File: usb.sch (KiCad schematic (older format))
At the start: 15 parts, among them J2 USB_OTG, Q1 BC817, U1 STMPS2151STR

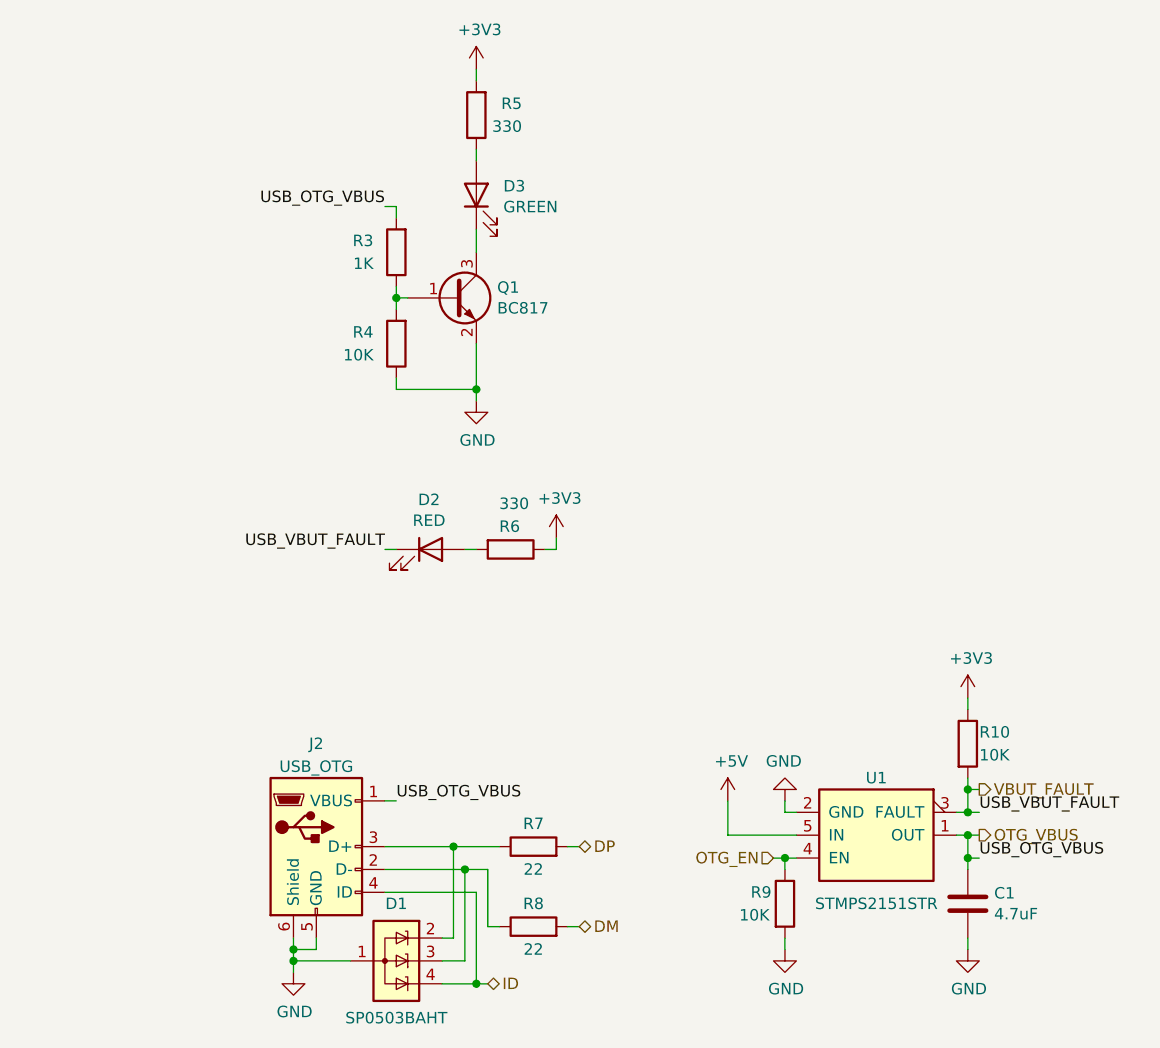
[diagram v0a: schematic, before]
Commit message: Запитал МК, добавил цепи питания, тактирования, модуль клавиатуры.
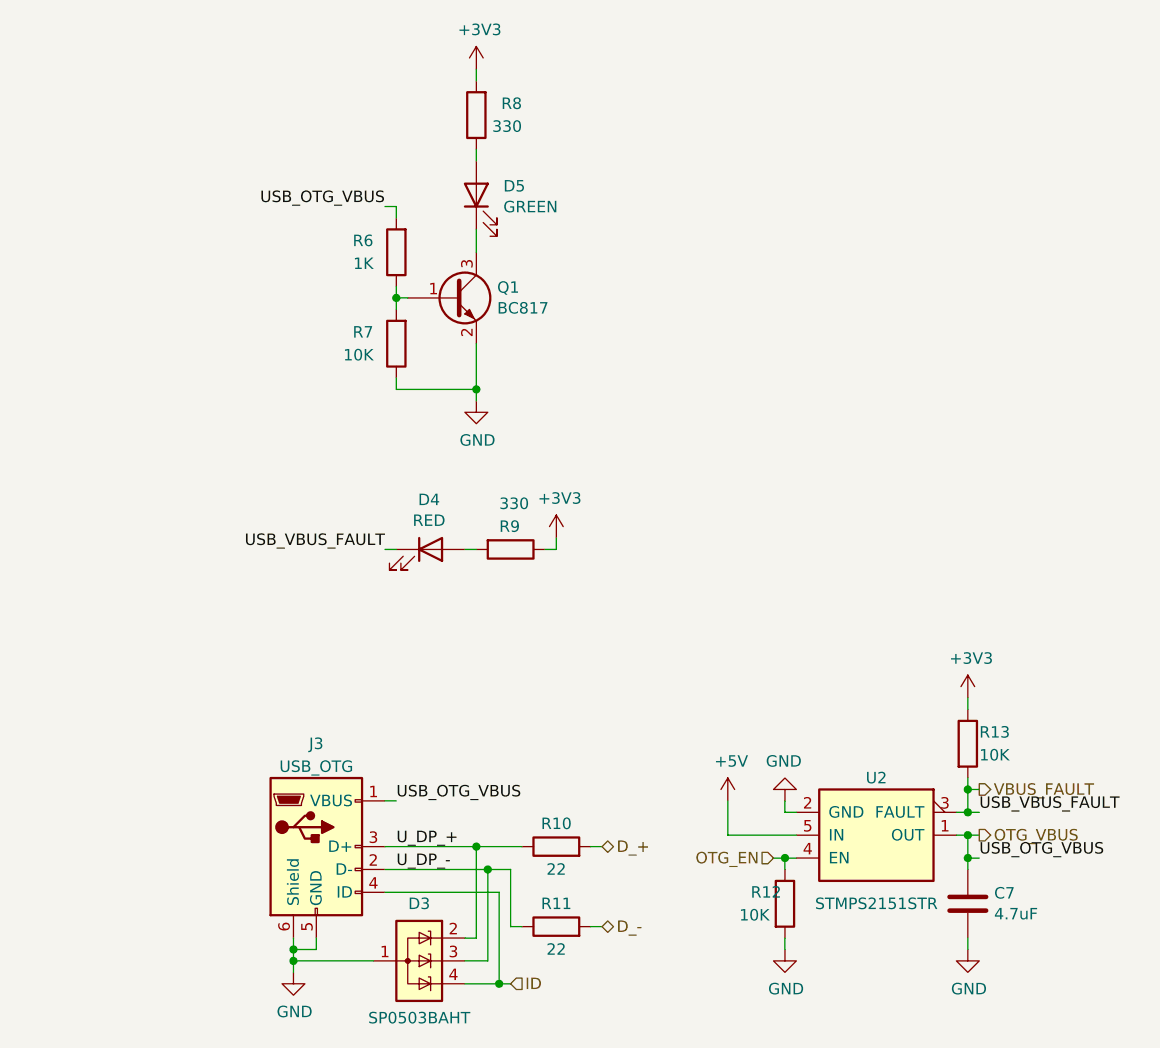
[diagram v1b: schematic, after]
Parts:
- renumbered C1 to C7, D1 to D3, D2 to D4, D3 to D5, J2 to J3, R7 to R10, R8 to R11, R9 to R12, R10 to R13, R3 to R6, R4 to R7, R5 to R8, R6 to R9, U1 to U2
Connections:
- net U_DP_-: now reaches D3.3 (K), J3.2 (D-), R11.1
- net U_DP_+: now reaches D3.2 (K), J3.3 (D+), R10.1
- net DM renamed D_-
- net DP renamed D_+
- net VBUT_FAULT renamed VBUS_FAULT
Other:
- moved on the sheet: D3, R10, R11
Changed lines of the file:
@@
 $Descr A4 11693 8268
 encoding utf-8
-Sheet 5 5
+Sheet 9 9
 Title ""
 Date ""
@@
 $EndDescr
 $Comp
-L interface_usb:STMPS2151STR U1
+L interface_usb:STMPS2151STR U2
 U 1 1 5EBF34AD
 P 6900 4550
-F 0 "U1" H 7150 4600 50  0000 C CNN
+F 0 "U2" H 7150 4600 50  0000 C CNN
 F 1 "STMPS2151STR" H 7150 4050 50  0000 C CNN
 F 2 "Package_TO_SOT_SMD:SOT-23-5_HandSoldering" H 6950 4600 50  0001 C CNN
@@
 $EndComp
 $Comp
-L power:GND #PWR014
+L power:GND #PWR017
 U 1 1 5EBF34B3
 P 6750 4600
-F 0 "#PWR014" H 6750 4350 50  0001 C CNN
+F 0 "#PWR017" H 6750 4350 50  0001 C CNN
 F 1 "GND" H 6755 4427 50  0000 C CNN
 F 2 "" H 6750 4600 50  0001 C CNN
@@
 	6750 4650 6750 4600
 $Comp
-L power:+5V #PWR013
+L power:+5V #PWR016
 U 1 1 5EBF34BB
 P 6500 4600
-F 0 "#PWR013" H 6500 4450 50  0001 C CNN
+F 0 "#PWR016" H 6500 4450 50  0001 C CNN
 F 1 "+5V" H 6515 4773 50  0000 C CNN
 F 2 "" H 6500 4600 50  0001 C CNN
@@
 	7500 4750 7550 4750
 $Comp
-L Device:R R9
+L Device:R R12
 U 1 1 5EBF34C5
 P 6750 5050
-F 0 "R9" H 6600 5100 50  0000 L CNN
+F 0 "R12" H 6600 5100 50  0000 L CNN
 F 1 "10K" H 6550 5000 50  0000 L CNN
 F 2 "Resistor_SMD:R_0603_1608Metric_Pad1.05x0.95mm_HandSolder" V 6680 5050 50  0001 C CNN
@@
 	6750 4850 6750 4900
 $Comp
-L power:GND #PWR015
+L power:GND #PWR018
 U 1 1 5EBF34CD
 P 6750 5250
-F 0 "#PWR015" H 6750 5000 50  0001 C CNN
+F 0 "#PWR018" H 6750 5000 50  0001 C CNN
 F 1 "GND" H 6755 5077 50  0000 C CNN
 F 2 "" H 6750 5250 50  0001 C CNN
@@
 Connection ~ 6750 4850
 $Comp
-L Device:C C1
+L Device:C C7
 U 1 1 5EBF34D7
 P 7550 5050
-F 0 "C1" H 7665 5096 50  0000 L CNN
+F 0 "C7" H 7665 5096 50  0000 L CNN
 F 1 "4.7uF" H 7665 5005 50  0000 L CNN
 F 2 "Capacitor_SMD:C_0603_1608Metric_Pad1.05x0.95mm_HandSolder" H 7588 4900 50  0001 C CNN
@@
 Connection ~ 7550 4750
 $Comp
-L power:GND #PWR017
+L power:GND #PWR020
 U 1 1 5EBF34E0
 P 7550 5250
-F 0 "#PWR017" H 7550 5000 50  0001 C CNN
+F 0 "#PWR020" H 7550 5000 50  0001 C CNN
 F 1 "GND" H 7555 5077 50  0000 C CNN
 F 2 "" H 7550 5250 50  0001 C CNN
@@
 	7500 4650 7550 4650
 $Comp
-L power:+3V3 #PWR016
+L power:+3V3 #PWR019
 U 1 1 5EBF34E9
 P 7550 4150
-F 0 "#PWR016" H 7550 4000 50  0001 C CNN
+F 0 "#PWR019" H 7550 4000 50  0001 C CNN
 F 1 "+3V3" H 7565 4323 50  0000 C CNN
 F 2 "" H 7550 4150 50  0001 C CNN
@@
 	7550 4150 7550 4200
 $Comp
-L Device:LED D2
+L Device:LED D4
 U 1 1 5EBF34F9
 P 5200 3500
-F 0 "D2" H 5193 3717 50  0000 C CNN
+F 0 "D4" H 5193 3717 50  0000 C CNN
 F 1 "RED" H 5193 3626 50  0000 C CNN
 F 2 "LED_SMD:LED_0603_1608Metric_Pad1.05x0.95mm_HandSolder" H 5200 3500 50  0001 C CNN
@@
 $EndComp
 $Comp
-L Device:R R6
+L Device:R R9
 U 1 1 5EBF34FF
 P 5550 3500
-F 0 "R6" V 5450 3450 50  0000 L CNN
+F 0 "R9" V 5450 3450 50  0000 L CNN
 F 1 "330" V 5350 3450 50  0000 L CNN
 F 2 "Resistor_SMD:R_0603_1608Metric_Pad1.05x0.95mm_HandSolder" V 5480 3500 50  0001 C CNN
@@
 $EndComp
 $Comp
-L power:+3V3 #PWR012
+L power:+3V3 #PWR015
 U 1 1 5EBF3506
 P 5750 3450
-F 0 "#PWR012" H 5750 3300 50  0001 C CNN
+F 0 "#PWR015" H 5750 3300 50  0001 C CNN
 F 1 "+3V3" H 5765 3623 50  0000 C CNN
 F 2 "" H 5750 3450 50  0001 C CNN
@@
 	5750 3500 5750 3450
 $Comp
-L Device:R R3
+L Device:R R6
 U 1 1 5EBF3510
 P 5050 2200
-F 0 "R3" H 5150 2150 50  0000 L CNN
+F 0 "R6" H 5150 2150 50  0000 L CNN
 F 1 "1K" H 5150 2250 50  0000 L CNN
 F 2 "Resistor_SMD:R_0603_1608Metric_Pad1.05x0.95mm_HandSolder" V 4980 2200 50  0001 C CNN
@@
 $EndComp
 $Comp
-L Device:R R4
+L Device:R R7
 U 1 1 5EBF3516
 P 5050 2600
-F 0 "R4" H 5150 2550 50  0000 L CNN
+F 0 "R7" H 5150 2550 50  0000 L CNN
 F 1 "10K" H 5150 2650 50  0000 L CNN
 F 2 "Resistor_SMD:R_0603_1608Metric_Pad1.05x0.95mm_HandSolder" V 4980 2600 50  0001 C CNN
@@
 $EndComp
 $Comp
-L Device:R R5
+L Device:R R8
 U 1 1 5EBF351C
 P 5400 1600
-F 0 "R5" H 5200 1550 50  0000 L CNN
+F 0 "R8" H 5200 1550 50  0000 L CNN
 F 1 "330" H 5200 1650 50  0000 L CNN
 F 2 "Resistor_SMD:R_0603_1608Metric_Pad1.05x0.95mm_HandSolder" V 5330 1600 50  0001 C CNN
@@
 Connection ~ 5050 2400
 $Comp
-L power:+3V3 #PWR010
+L power:+3V3 #PWR013
 U 1 1 5EBF352C
 P 5400 1400
-F 0 "#PWR010" H 5400 1250 50  0001 C CNN
+F 0 "#PWR013" H 5400 1250 50  0001 C CNN
 F 1 "+3V3" H 5415 1573 50  0000 C CNN
 F 2 "" H 5400 1400 50  0001 C CNN
@@
 	5400 1400 5400 1450
 $Comp
-L Device:LED D3
+L Device:LED D5
 U 1 1 5EBF3533
 P 5400 1950
-F 0 "D3" V 5439 1832 50  0000 R CNN
+F 0 "D5" V 5439 1832 50  0000 R CNN
 F 1 "GREEN" V 5348 1832 50  0000 R CNN
 F 2 "LED_SMD:LED_0603_1608Metric_Pad1.05x0.95mm_HandSolder" H 5400 1950 50  0001 C CNN
@@
 	5400 2100 5400 2200
 $Comp
-L power:GND #PWR011
+L power:GND #PWR014
 U 1 1 5EBF3541
 P 5400 2850
-F 0 "#PWR011" H 5400 2600 50  0001 C CNN
+F 0 "#PWR014" H 5400 2600 50  0001 C CNN
 F 1 "GND" H 5405 2677 50  0000 C CNN
 F 2 "" H 5400 2850 50  0001 C CNN
@@
 	5050 2000 5050 2050
 $Comp
-L Connector:USB_OTG J2
+L Connector:USB_OTG J3
 U 1 1 5EBF354C
 P 4700 4800
-F 0 "J2" H 4700 5250 50  0000 C CNN
+F 0 "J3" H 4700 5250 50  0000 C CNN
 F 1 "USB_OTG" H 4700 5150 50  0000 C CNN
 F 2 "Connector_USB:USB_Mini-B_Wuerth_65100516121_Horizontal" H 4850 4750 50  0001 C CNN
@@
 $EndComp
 Wire Wire Line
-	5000 4800 5300 4800
-Wire Wire Line
-	5300 5200 5300 4800
-Connection ~ 5300 4800
-Wire Wire Line
-	5300 4800 5500 4800
+	5000 4800 5400 4800
+Wire Wire Line
+	5400 5200 5400 4800
+Connection ~ 5400 4800
+Wire Wire Line
+	5400 4800 5600 4800
 Connection ~ 4600 5300
 Wire Wire Line
 	4600 5350 4600 5300
 Wire Wire Line
-	4600 5300 4850 5300
-Wire Wire Line
-	5350 4900 5450 4900
-Connection ~ 5350 4900
-Wire Wire Line
-	5350 5300 5350 4900
-Wire Wire Line
-	5250 5300 5350 5300
-Wire Wire Line
-	5250 5200 5300 5200
-Connection ~ 5400 5400
-Wire Wire Line
-	5250 5400 5400 5400
-Wire Wire Line
-	5000 5000 5400 5000
-Wire Wire Line
-	5400 5400 5450 5400
-Wire Wire Line
-	5400 5000 5400 5400
-Wire Wire Line
-	5800 5150 5850 5150
-Wire Wire Line
-	5800 4800 5850 4800
-Wire Wire Line
-	5450 5150 5500 5150
-Wire Wire Line
-	5450 4900 5450 5150
-Wire Wire Line
-	5000 4900 5350 4900
-$Comp
-L Device:R R7
+	4600 5300 4950 5300
+Wire Wire Line
+	5450 4900 5550 4900
+Connection ~ 5450 4900
+Wire Wire Line
+	5450 5300 5450 4900
+Connection ~ 5500 5400
+Wire Wire Line
+	5350 5400 5500 5400
+Wire Wire Line
+	5000 5000 5500 5000
+Wire Wire Line
+	5500 5400 5550 5400
+Wire Wire Line
+	5500 5000 5500 5400
+Wire Wire Line
+	5900 5150 5950 5150
+Wire Wire Line
+	5900 4800 5950 4800
+Wire Wire Line
+	5550 5150 5600 5150
+Wire Wire Line
+	5550 4900 5550 5150
+Wire Wire Line
+	5000 4900 5450 4900
+$Comp
+L Device:R R10
 U 1 1 5EBF356B
-P 5650 4800
-F 0 "R7" V 5750 4800 50  0000 C CNN
-F 1 "22" V 5550 4800 50  0000 C CNN
-F 2 "Resistor_SMD:R_0603_1608Metric_Pad1.05x0.95mm_HandSolder" V 5580 4800 50  0001 C CNN
-F 3 "~" H 5650 4800 50  0001 C CNN
-	1    5650 4800
+P 5750 4800
+F 0 "R10" V 5850 4800 50  0000 C CNN
+F 1 "22" V 5650 4800 50  0000 C CNN
+F 2 "Resistor_SMD:R_0603_1608Metric_Pad1.05x0.95mm_HandSolder" V 5680 4800 50  0001 C CNN
+F 3 "~" H 5750 4800 50  0001 C CNN
+	1    5750 4800
 	0    -1   -1   0
 $EndComp
@@
 	4600 5300 4600 5250
 $Comp
-L power:GND #PWR08
+L power:GND #PWR012
 U 1 1 5EBF3573
 P 4600 5350
-F 0 "#PWR08" H 4600 5100 50  0001 C CNN
+F 0 "#PWR012" H 4600 5100 50  0001 C CNN
 F 1 "GND" H 4605 5177 50  0000 C CNN
 F 2 "" H 4600 5350 50  0001 C CNN
@@
 	4600 5200 4600 5250
 $Comp
-L Power_Protection:SP0503BAHT D1
+L Power_Protection:SP0503BAHT D3
 U 1 1 5EBF357C
-P 5050 5300
-F 0 "D1" V 4800 5300 50  0000 C CNN
-F 1 "SP0503BAHT" V 5300 5300 50  0000 C CNN
-F 2 "Package_TO_SOT_SMD:SOT-143_Handsoldering" H 5275 5250 50  0001 L CNN
-F 3 "http://www.littelfuse.com/~/media/files/littelfuse/technical%20resources/documents/data%20sheets/sp05xxba.pdf" H 5175 5425 50  0001 C CNN
-	1    5050 5300
+P 5150 5300
+F 0 "D3" V 4900 5300 50  0000 C CNN
+F 1 "SP0503BAHT" V 5400 5300 50  0000 C CNN
+F 2 "Package_TO_SOT_SMD:SOT-143_Handsoldering" H 5375 5250 50  0001 L CNN
+F 3 "http://www.littelfuse.com/~/media/files/littelfuse/technical%20resources/documents/data%20sheets/sp05xxba.pdf" H 5275 5425 50  0001 C CNN
+	1    5150 5300
 	0    1    1    0
 $EndComp
 $Comp
-L Device:R R8
+L Device:R R11
 U 1 1 5EBF3583
-P 5650 5150
-F 0 "R8" V 5750 5150 50  0000 C CNN
-F 1 "22" V 5550 5150 50  0000 C CNN
-F 2 "Resistor_SMD:R_0603_1608Metric_Pad1.05x0.95mm_HandSolder" V 5580 5150 50  0001 C CNN
-F 3 "~" H 5650 5150 50  0001 C CNN
-	1    5650 5150
+P 5750 5150
+F 0 "R11" V 5850 5150 50  0000 C CNN
+F 1 "22" V 5650 5150 50  0000 C CNN
+F 2 "Resistor_SMD:R_0603_1608Metric_Pad1.05x0.95mm_HandSolder" V 5680 5150 50  0001 C CNN
+F 3 "~" H 5750 5150 50  0001 C CNN
+	1    5750 5150
 	0    -1   -1   0
 $EndComp
@@
 	5000 4600 5050 4600
 Text HLabel 7600 4550 2    50   Output ~ 0
-VBUT_FAULT
+VBUS_FAULT
 Text HLabel 7600 4750 2    50   Output ~ 0
 OTG_VBUS
@@
 Text Label 5050 4600 0    50   ~ 0
 USB_OTG_VBUS
-Text HLabel 5850 4800 2    50   BiDi ~ 0
-DP
-Text HLabel 5850 5150 2    50   BiDi ~ 0
-DM
-Text HLabel 5450 5400 2    50   BiDi ~ 0
+Text HLabel 5950 4800 2    50   BiDi ~ 0
+D_+
+Text HLabel 5950 5150 2    50   BiDi ~ 0
+D_-
+Text HLabel 5550 5400 2    50   Input ~ 0
 ID
 Text Label 7600 4650 0    50   ~ 0
-USB_VBUT_FAULT
+USB_VBUS_FAULT
 Wire Wire Line
 	7550 4550 7550 4650
@@
 	7550 4550 7600 4550
 $Comp
-L Device:R R10
+L Device:R R13
 U 1 1 5EBF34F3
 P 7550 4350
-F 0 "R10" H 7600 4400 50  0000 L CNN
+F 0 "R13" H 7600 4400 50  0000 L CNN
 F 1 "10K" H 7600 4300 50  0000 L CNN
 F 2 "Resistor_SMD:R_0603_1608Metric_Pad1.05x0.95mm_HandSolder" V 7480 4350 50  0001 C CNN
@@
 OTG_EN
 Text Label 5000 3500 2    50   ~ 0
-USB_VBUT_FAULT
+USB_VBUS_FAULT
 Text Label 5000 2000 2    50   ~ 0
 USB_OTG_VBUS
@@
 	5400 2800 5400 2850
 Connection ~ 5400 2800
+Text Label 5050 4800 0    50   ~ 0
+U_DP_+
+Text Label 5050 4900 0    50   ~ 0
+U_DP_-
+Wire Wire Line
+	5350 5300 5450 5300
+Wire Wire Line
+	5350 5200 5400 5200
 $EndSCHEMATC
